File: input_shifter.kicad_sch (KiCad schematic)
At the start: 4 parts

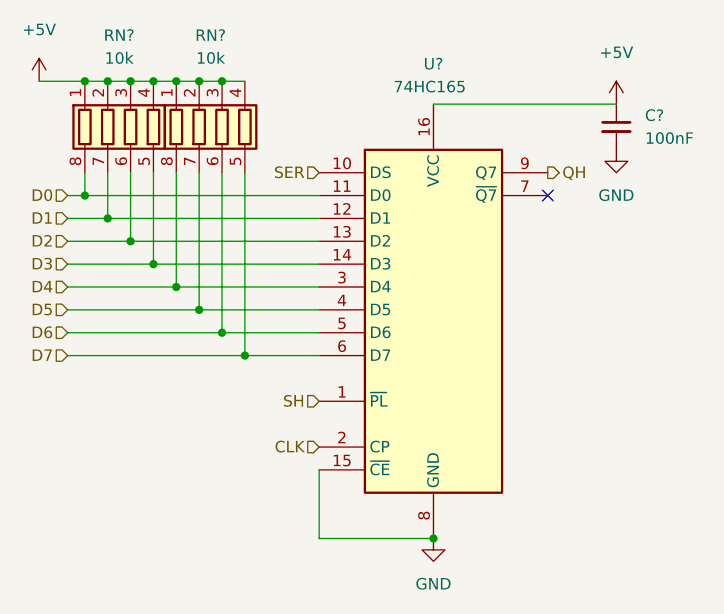
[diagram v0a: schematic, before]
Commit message: Added pico
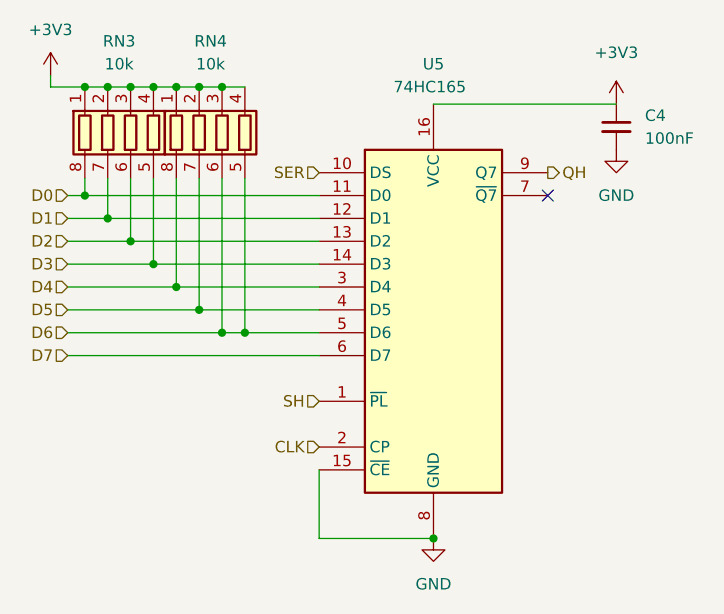
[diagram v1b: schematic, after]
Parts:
- gave numbers to parts that had none: 4
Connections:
- net D6: now also RN4.5 (R4.2)
- net D7: no longer RN4.5 (R4.2)
- net +5V renamed +3V3
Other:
- moved on the sheet: RN3, RN4

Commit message: Full schematic done
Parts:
- C4: value 100nF -> 10uF; footprint (none) -> Capacitor_SMD:C_0603_1608Metric
- RN3, RN4: footprint Resistor_SMD:R_Array_Convex_4x0603 -> CJ4-Autopilot:SW_PUSH_6mm
- U5: footprint (none) -> Package_SO:SOIC-16_3.9x9.9mm_P1.27mm; JLC (none) -> SOIC-16_3.9x9.9x1.27P; LCSC (none) -> C5613
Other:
- title: (none) -> CJ4 Autopilot Panel
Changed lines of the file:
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@@
 (kicad_sch (version 20211123) (generator eeschema)
   (paper "A4")
+  (title_block
+    (title "CJ4 Autopilot Panel")
+    (date "2022-08-25")
+    (rev "1.0.0")
+    (comment 1 "neile@live.com")
+    (comment 2 "Neil Enns")
+  )
   (junction (at 72.39 59.055) (diameter 0) (color 0 0 0 0)
   )
@@
   (symbol (lib_id "power:GND") (at 131.445 53.975 0)
     (in_bom yes) (on_board yes) (fields_autoplaced)
-    (property "Reference" "#PWR023" (id 0) (at 131.445 60.325 0)
+    (property "Reference" "#PWR024" (id 0) (at 131.445 60.325 0)
       (effects (font (size 1.27 1.27)) hide)
     )
@@
     (property "Reference" "RN3" (id 0) (at 76.2 41.91 0))
     (property "Value" "10k" (id 1) (at 76.2 44.45 0))
-    (property "Footprint" "Resistor_SMD:R_Array_Convex_4x0603" (id 2) (at 84.455 52.07 90)
+    (property "Footprint" "CJ4-Autopilot:SW_PUSH_6mm" (id 2) (at 84.455 52.07 90)
       (effects (font (size 1.27 1.27)) hide)
     )
@@
   (symbol (lib_id "power:+3V3") (at 131.445 48.895 0)
     (in_bom yes) (on_board yes) (fields_autoplaced)
-    (property "Reference" "#PWR022" (id 0) (at 131.445 52.705 0)
+    (property "Reference" "#PWR023" (id 0) (at 131.445 52.705 0)
       (effects (font (size 1.27 1.27)) hide)
     )
@@
       (effects (font (size 1.27 1.27)) (justify left))
     )
-    (property "Value" "100nF" (id 1) (at 134.62 52.7112 0)
+    (property "Value" "10uF" (id 1) (at 134.62 52.7112 0)
       (effects (font (size 1.27 1.27)) (justify left))
     )
-    (property "Footprint" "" (id 2) (at 131.445 51.435 0)
+    (property "Footprint" "Capacitor_SMD:C_0603_1608Metric" (id 2) (at 131.445 51.435 0)
       (effects (font (size 1.27 1.27)) hide)
     )
@@
     (property "Reference" "RN4" (id 0) (at 86.36 41.91 0))
     (property "Value" "10k" (id 1) (at 86.36 44.45 0))
-    (property "Footprint" "Resistor_SMD:R_Array_Convex_4x0603" (id 2) (at 94.615 52.07 90)
+    (property "Footprint" "CJ4-Autopilot:SW_PUSH_6mm" (id 2) (at 94.615 52.07 90)
       (effects (font (size 1.27 1.27)) hide)
     )
@@
   (symbol (lib_id "power:GND") (at 111.125 97.155 0)
     (in_bom yes) (on_board yes) (fields_autoplaced)
-    (property "Reference" "#PWR021" (id 0) (at 111.125 103.505 0)
+    (property "Reference" "#PWR022" (id 0) (at 111.125 103.505 0)
       (effects (font (size 1.27 1.27)) hide)
     )
@@
       (effects (font (size 1.27 1.27)) (justify left))
     )
-    (property "Footprint" "" (id 2) (at 111.125 71.755 0)
+    (property "Footprint" "Package_SO:SOIC-16_3.9x9.9mm_P1.27mm" (id 2) (at 111.125 71.755 0)
       (effects (font (size 1.27 1.27)) hide)
     )
     (property "Datasheet" "https://assets.nexperia.com/documents/data-sheet/74HC_HCT165.pdf" (id 3) (at 111.125 71.755 0)
+      (effects (font (size 1.27 1.27)) hide)
+    )
+    (property "JLC" "SOIC-16_3.9x9.9x1.27P" (id 4) (at 111.125 71.755 0)
+      (effects (font (size 1.27 1.27)) hide)
+    )
+    (property "LCSC" "C5613" (id 5) (at 111.125 71.755 0)
       (effects (font (size 1.27 1.27)) hide)
     )
@@
   (symbol (lib_id "power:+3V3") (at 68.58 45.72 0)
     (in_bom yes) (on_board yes) (fields_autoplaced)
-    (property "Reference" "#PWR020" (id 0) (at 68.58 49.53 0)
-      (effects (font (size 1.27 1.27)) hide)
-    )
+    (property "Reference" "#PWR021" (id 0) (at 68.58 49.53 0)
+      (effects (font (size 1.27 1.27)) hide)
+    )
